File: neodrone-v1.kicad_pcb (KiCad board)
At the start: 4 copper layers, 150 x 105 mm, 20 parts, among them U1 ATSAMD21G18A-A

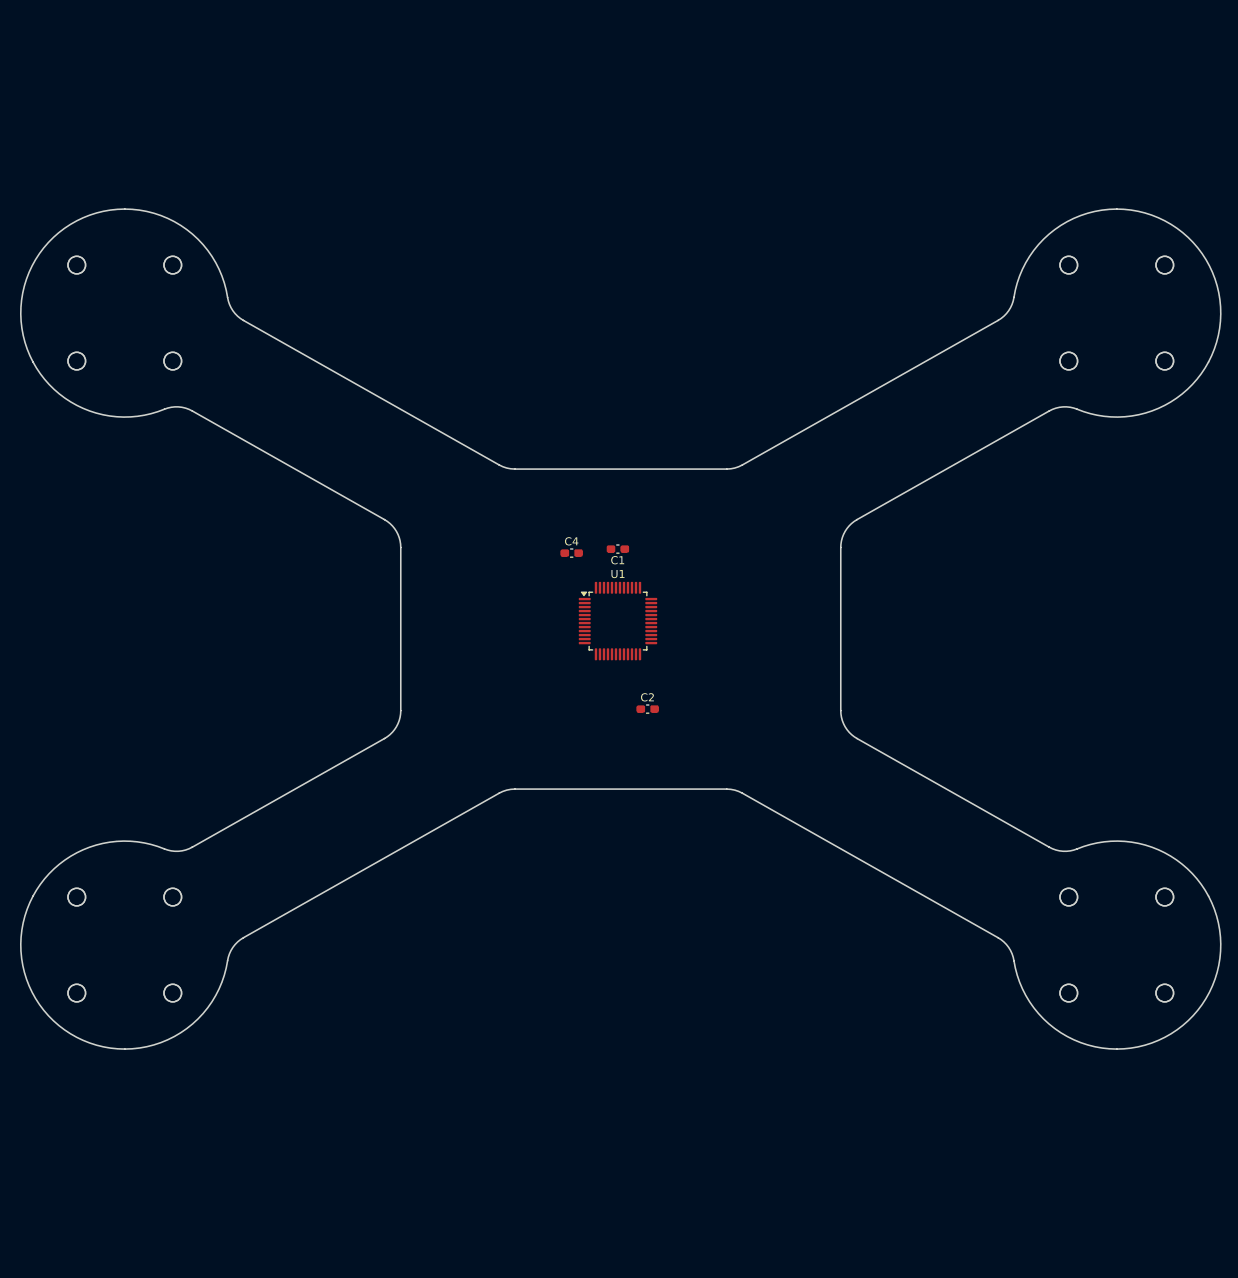
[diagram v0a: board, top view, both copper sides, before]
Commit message: imu, motor esc schematics
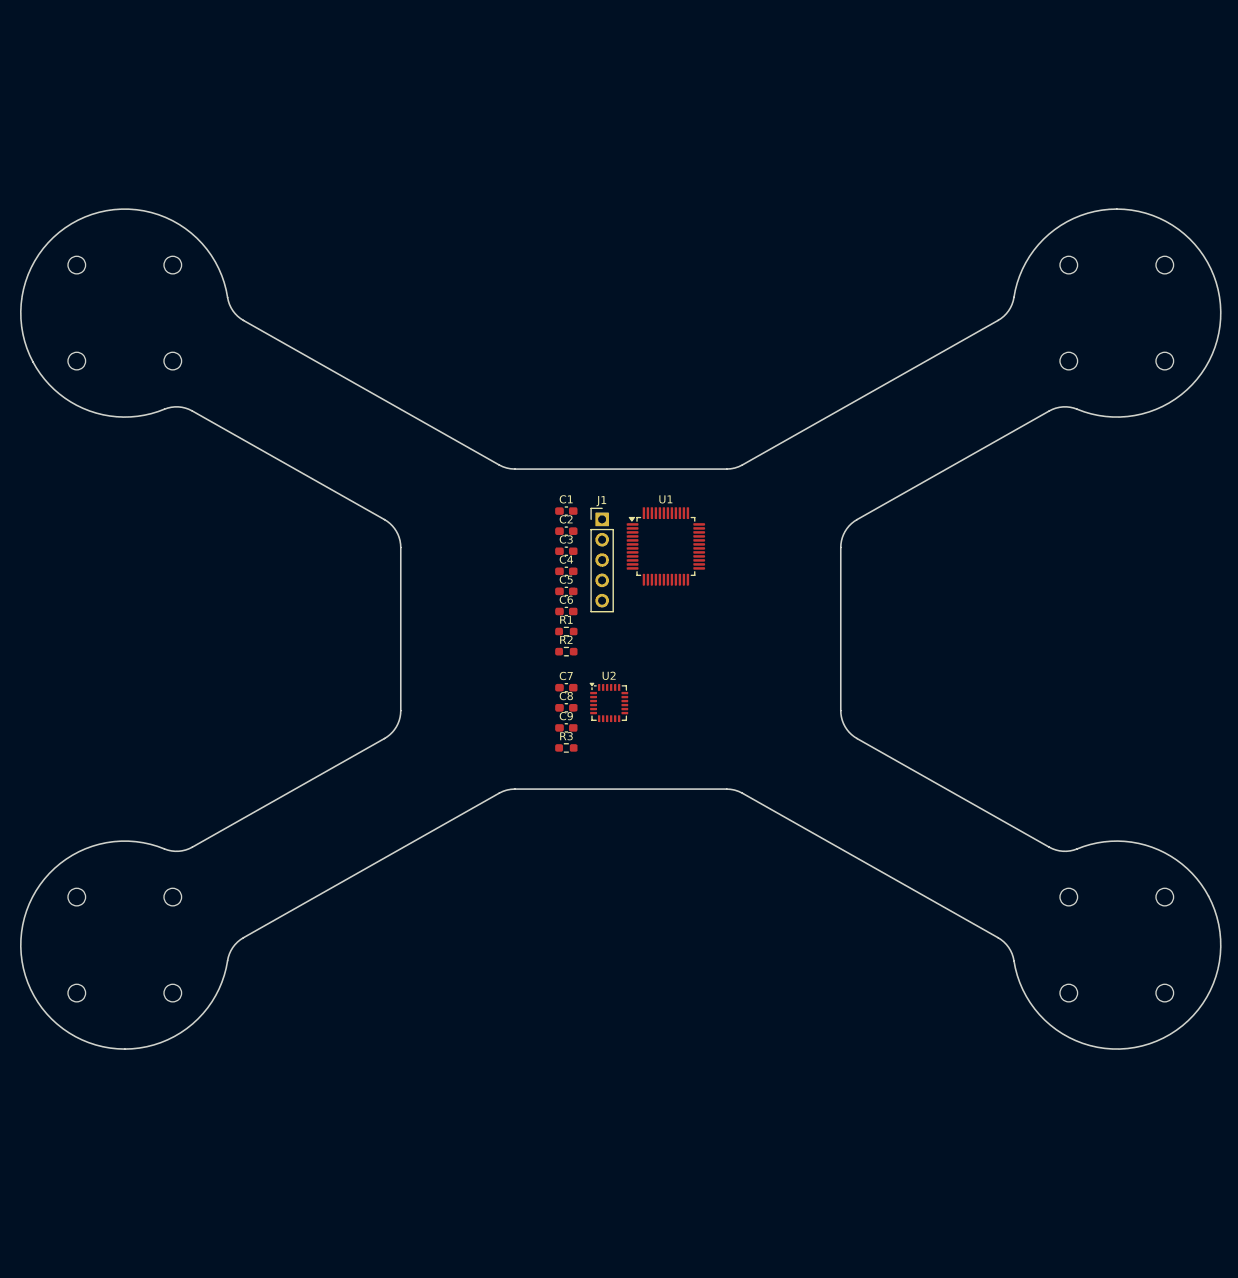
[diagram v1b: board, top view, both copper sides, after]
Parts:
- added C3: 100nF, Capacitor_SMD:C_0603_1608Metric_Pad1.08x0.95mm_HandSolder, F.Cu at (143.7, 90.3)
- added C5: 100nF, Capacitor_SMD:C_0603_1608Metric_Pad1.08x0.95mm_HandSolder, F.Cu at (143.7, 95.3)
- added C6: 4.7uF, Capacitor_SMD:C_0603_1608Metric_Pad1.08x0.95mm_HandSolder, F.Cu at (143.7, 97.8)
- added C7: 100nF, Capacitor_SMD:C_0603_1608Metric_Pad1.08x0.95mm_HandSolder, F.Cu at (143.7, 107.3)
- added C8: 100nF, Capacitor_SMD:C_0603_1608Metric_Pad1.08x0.95mm_HandSolder, F.Cu at (143.7, 109.8)
- added C9: 2.2nF, Capacitor_SMD:C_0603_1608Metric_Pad1.08x0.95mm_HandSolder, F.Cu at (143.7, 112.3)
- added J1: Conn_01x05_Socket, Connector_PinHeader_2.54mm:PinHeader_1x05_P2.54mm_Vertical, F.Cu at (148.2, 86.3)
- added R1: 10k, Resistor_SMD:R_0603_1608Metric_Pad0.98x0.95mm_HandSolder, F.Cu at (143.7, 100.3)
- added R2: 33, Resistor_SMD:R_0603_1608Metric_Pad0.98x0.95mm_HandSolder, F.Cu at (143.7, 102.8)
- added R3: 10k, Resistor_SMD:R_0603_1608Metric_Pad0.98x0.95mm_HandSolder, F.Cu at (143.7, 114.9)
- added U2: MPU-6000, Sensor_Motion:InvenSense_QFN-24_4x4mm_P0.5mm, F.Cu at (149.1, 109.2)
- moved C2 24.5 mm to (143.7, 87.8)
- moved U1 11.1 mm to (156.1, 89.7)
- moved C1 8.00 mm to (143.7, 85.2), turned to 0 degrees
- moved C4 2.37 mm to (143.7, 92.8)
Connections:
- C2 pad 1: unconnected-(C2-Pad1) -> +3V3
- C2 pad 2: Net-(C2-Pad2) -> GND
- C4 pad 1: unconnected-(C4-Pad1) -> +3V3
- C4 pad 2: Net-(U1-VDDIN) -> GND
- U1 pad 13: unconnected-(U1-PA08-Pad13) -> /mcu/I2C_SDA
- U1 pad 14: unconnected-(U1-PA09-Pad14) -> /mcu/I2C_SCL
- U1 pad 15: unconnected-(U1-PA10-Pad15) -> /mcu/CRSF_TX
- U1 pad 16: unconnected-(U1-PA11-Pad16) -> /mcu/CRSF_RX
- U1 pad 17: unconnected-(U1-VDDIO-Pad17) -> +3V3
- U1 pad 19: unconnected-(U1-PB10-Pad19) -> IMU_MOSI
- U1 pad 20: unconnected-(U1-PB11-Pad20) -> IMU_SCK
- U1 pad 21: unconnected-(U1-PA12-Pad21) -> IMU_MISO
- U1 pad 22: unconnected-(U1-PA13-Pad22) -> IMU_CS
- U1 pad 23: unconnected-(U1-PA14-Pad23) -> IMU_INT
- U1 pad 25: unconnected-(U1-PA16-Pad25) -> /mcu/M1_PWM
- U1 pad 26: unconnected-(U1-PA17-Pad26) -> /mcu/M2_PWM
- U1 pad 27: unconnected-(U1-PA18-Pad27) -> /mcu/M3_PWM
- U1 pad 28: unconnected-(U1-PA19-Pad28) -> /mcu/M4_PWM
- U1 pad 33: unconnected-(U1-PA24-Pad33) -> /mcu/USB_DM
- U1 pad 34: unconnected-(U1-PA25-Pad34) -> /mcu/USB_DP
- U1 pad 36: Net-(C2-Pad2) -> +3V3
- U1 pad 40: unconnected-(U1-~{RESET}-Pad40) -> Net-(J1-RESET)
- U1 pad 44: Net-(U1-VDDIN) -> +3V3
- U1 pad 45: unconnected-(U1-PA30-Pad45) -> Net-(J1-SWDIO)
- U1 pad 46: unconnected-(U1-PA31-Pad46) -> Net-(U1-PA31)
- U1 pad 6: unconnected-(U1-VDDANA-Pad6) -> +3V3
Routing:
- added copper zone on In1.Cu, net GND
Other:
- outline, holes or cut-outs redrawn

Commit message: more esc schematics, refactoring, root schematic edits
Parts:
- added C10: 22uF, Capacitor_SMD:C_1206_3216Metric_Pad1.33x1.80mm_HandSolder, F.Cu at (130.2, 80.1)
- added C11: 100nF, Capacitor_SMD:C_0603_1608Metric_Pad1.08x0.95mm_HandSolder, F.Cu at (125.0, 79.7)
- added C12: 47nF, Capacitor_SMD:C_0603_1608Metric_Pad1.08x0.95mm_HandSolder, F.Cu at (125.0, 82.2)
- added C13: 1uF, Capacitor_SMD:C_0603_1608Metric_Pad1.08x0.95mm_HandSolder, F.Cu at (125.0, 84.7)
- added C14: 1uF, Capacitor_SMD:C_0603_1608Metric_Pad1.08x0.95mm_HandSolder, F.Cu at (125.0, 87.2)
- added C15: 1uF, Capacitor_SMD:C_0603_1608Metric_Pad1.08x0.95mm_HandSolder, F.Cu at (125.0, 89.7)
- added C16: 22uF, Capacitor_SMD:C_1206_3216Metric_Pad1.33x1.80mm_HandSolder, F.Cu at (130.2, 83.5)
- added L1: 2.2uH, Inductor_SMD:L_1008_2520Metric_Pad1.43x2.20mm_HandSolder, F.Cu at (129.8, 87.0)
- C2, C3, C4, C5, C6: moved to B.Cu
- moved C6 30.0 mm to (172.5, 89.4), turned to 90 degrees
- moved J1 29.8 mm to (175.5, 98.1), turned to 180 degrees
- moved R2 29.2 mm to (172.0, 95.5), turned to 180 degrees
- moved R1 20.2 mm to (154.2, 83.1), turned to 180 degrees
- moved R3 15.2 mm to (152.5, 102.5), turned to 180 degrees
- moved C8 13.3 mm to (157.0, 110.7), turned to 180 degrees
- moved C5 11.5 mm to (154.3, 90.9), turned to -90 degrees
- moved C7 11.3 mm to (151.5, 115.5), turned to -90 degrees
- moved C9 11.1 mm to (152.0, 105.0), turned to 90 degrees
- moved C2 9.06 mm to (150.3, 94.0), turned to 180 degrees
- moved C1 7.99 mm to (151.7, 84.8), turned to -90 degrees
- moved C3 7.64 mm to (151.1, 92.0)
- moved C4 7.14 mm to (150.3, 90.0), turned to 180 degrees
- moved U1 4.67 mm to (151.9, 91.7)
- moved U2 2.21 mm to (151.2, 109.5)
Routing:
- net +3V3: track 0.00 -> 93.5 mm, vias 0 -> 7
- net Net-(J1-RESET): track 0.00 -> 51.7 mm
- net Net-(J1-SWDIO): track 0.00 -> 46.4 mm
- net GND: track 0.00 -> 45.7 mm, vias 0 -> 8
- net Net-(U1-PA31): track 0.00 -> 40.7 mm
- net IMU_INT: track 0.00 -> 25.1 mm
- net IMU_MISO: track 0.00 -> 21.5 mm
- net IMU_CS: track 0.00 -> 21.3 mm
- net IMU_SCK: track 0.00 -> 12.6 mm, vias 0 -> 2
- net IMU_MOSI: track 0.00 -> 12.6 mm, vias 0 -> 2
- net Net-(U2-REGOUT): track 0.00 -> 3.24 mm
- net Net-(J1-SWCLK): track 0.00 -> 2.62 mm
- net Net-(U1-VDDCORE): track 0.00 -> 1.86 mm
- net Net-(U2-CPOUT): track 0.00 -> 1.64 mm
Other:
- board text added: "1uF"
